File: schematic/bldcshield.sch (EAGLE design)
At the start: 39 parts, among them IC1 IR2101SMD, IC2 IR2101SMD, IC3 IR2101SMD, Q1 MOSFET-NCHANNELFDD8580, Q2 MOSFET-NCHANNELFDD8580, Q3 Shield, Q4 MOSFET-NCHANNELFDD8580, Q5 MOSFET-NCHANNELFDD8580, Q6 MOSFET-NCHANNELFDD8580, Q7 MOSFET-NCHANNELFDD8580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

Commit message: created new shield version in schematic based off lessons from Chinese controller.
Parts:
- removed JP1: (no value), SparkFun-Connectors:PINHD-2X3
- removed Q7: MOSFET-NCHANNELFDD8580, SparkFun:MOSFET-NCHANNELFDD8580
- removed U3: LM317DCY, Texas Instruments_By_element14_Batch_1:LM317DCY
- removed X1: MKDSN1,5/2-5,08, con-phoenix-508:MKDSN1,5/2-5,08
- removed X2: MKDSN1,5/3-5,08, con-phoenix-508:MKDSN1,5/3-5,08
- added +: Vcc, wirepad:3,81/1,4
- added -, BLDC1, BLDC2, BLDC3: (no value), wirepad:3,81/1,4
- added C3: 1000uF, SparkFun-Passives:CAP_POLPTH3
- added J1: (no value), SparkFun-Connectors:M02PTH
- added Q8: Shield, adafruit:ARDUINOR3-NOIOREF-NOTEXT
- added U1: V_REG_317SINK, SparkFun-PowerIC:V_REG_317SINK
- Q1, Q2, Q4, Q5, Q6: value MOSFET-NCHANNELFDD8580 -> BUZ11BV; device SparkFun:MOSFET-NCHANNELFDD8580 -> transistor-power:BUZ11BV
- Q3: value Shield -> BUZ11BV; device adafruit:ARDUINOR3-NOIOREF-NOTEXT -> transistor-power:BUZ11BV
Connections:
- removed net +3V3: Q3.3V
- removed net HI_1: IC1.HIN, Q3.D13
- removed net LO_1: IC1.LIN, Q3.D12
- removed net N$10: JP1.4, Q3.A1, R5.1
- new net N$2: R32.2, R33.1, U1.ADJ
- new net N$6: Q8.D2, R7.1
- new net N$8: IC1.LIN, Q8.D12
- net +12V: now also U1.OUT; no longer U3.OUTPUT, U3.OUTPUT_2
- net +5V: now also J1.2, Q8.5V; no longer JP1.1, Q3.5V, Q3.VIN
- net BLDC1: now also BLDC1.P; no longer X2-1.KL
- net BLDC2: now also BLDC2.P, Q3.S, Q4.D; no longer Q4.S, Q5.D, X2-2.KL
- net BLDC3: now also BLDC3.P, Q5.S, Q6.D; no longer Q6.S, Q7.D, X2-3.KL
- net CURRENT: now also Q4.S, Q6.S, Q8.A1; no longer Q3.A4/SDA, Q5.S, Q7.S
- net GND: now also -.P, C3.-, J1.1, Q8.GND, Q8.GND1, Q8.GND2; no longer JP1.5, Q3.GND, Q3.GND1, Q3.GND2, X1-2.KL
- net HI_2: now also Q8.D9; no longer Q3.D11
- net HI_3: now also Q8.D5; no longer Q3.D9
- net LOW_VOLTAGE: now also Q8.A0; no longer Q3.A3
- net LO_2: now also Q8.D8; no longer Q3.D10
- net LO_3: now also Q8.D13; no longer Q3.D8
- net N$1: now also Q3.G; no longer Q4.G
- net N$14: now also Q5.G; no longer Q6.G
- net N$15: now also Q6.G; no longer Q7.G
- net N$23: now also Q4.G; no longer Q5.G
- net N$4: now also IC1.HIN, Q8.D4; no longer JP1.2, Q3.A2, R7.1
- net N$5: now also Q8.D1, R5.1; no longer R32.2, R33.1, U3.ADJUST
- net N$7: now also Q8.D0; no longer JP1.6, Q3.A0
- net VCC: now also +.P, C3.+, Q3.D, Q5.D, U1.IN; no longer Q4.D, Q6.D, U3.INPUT, X1-1.KL
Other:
- moved on the sheet: C24, C25, R32, R33, R4, R5, R7

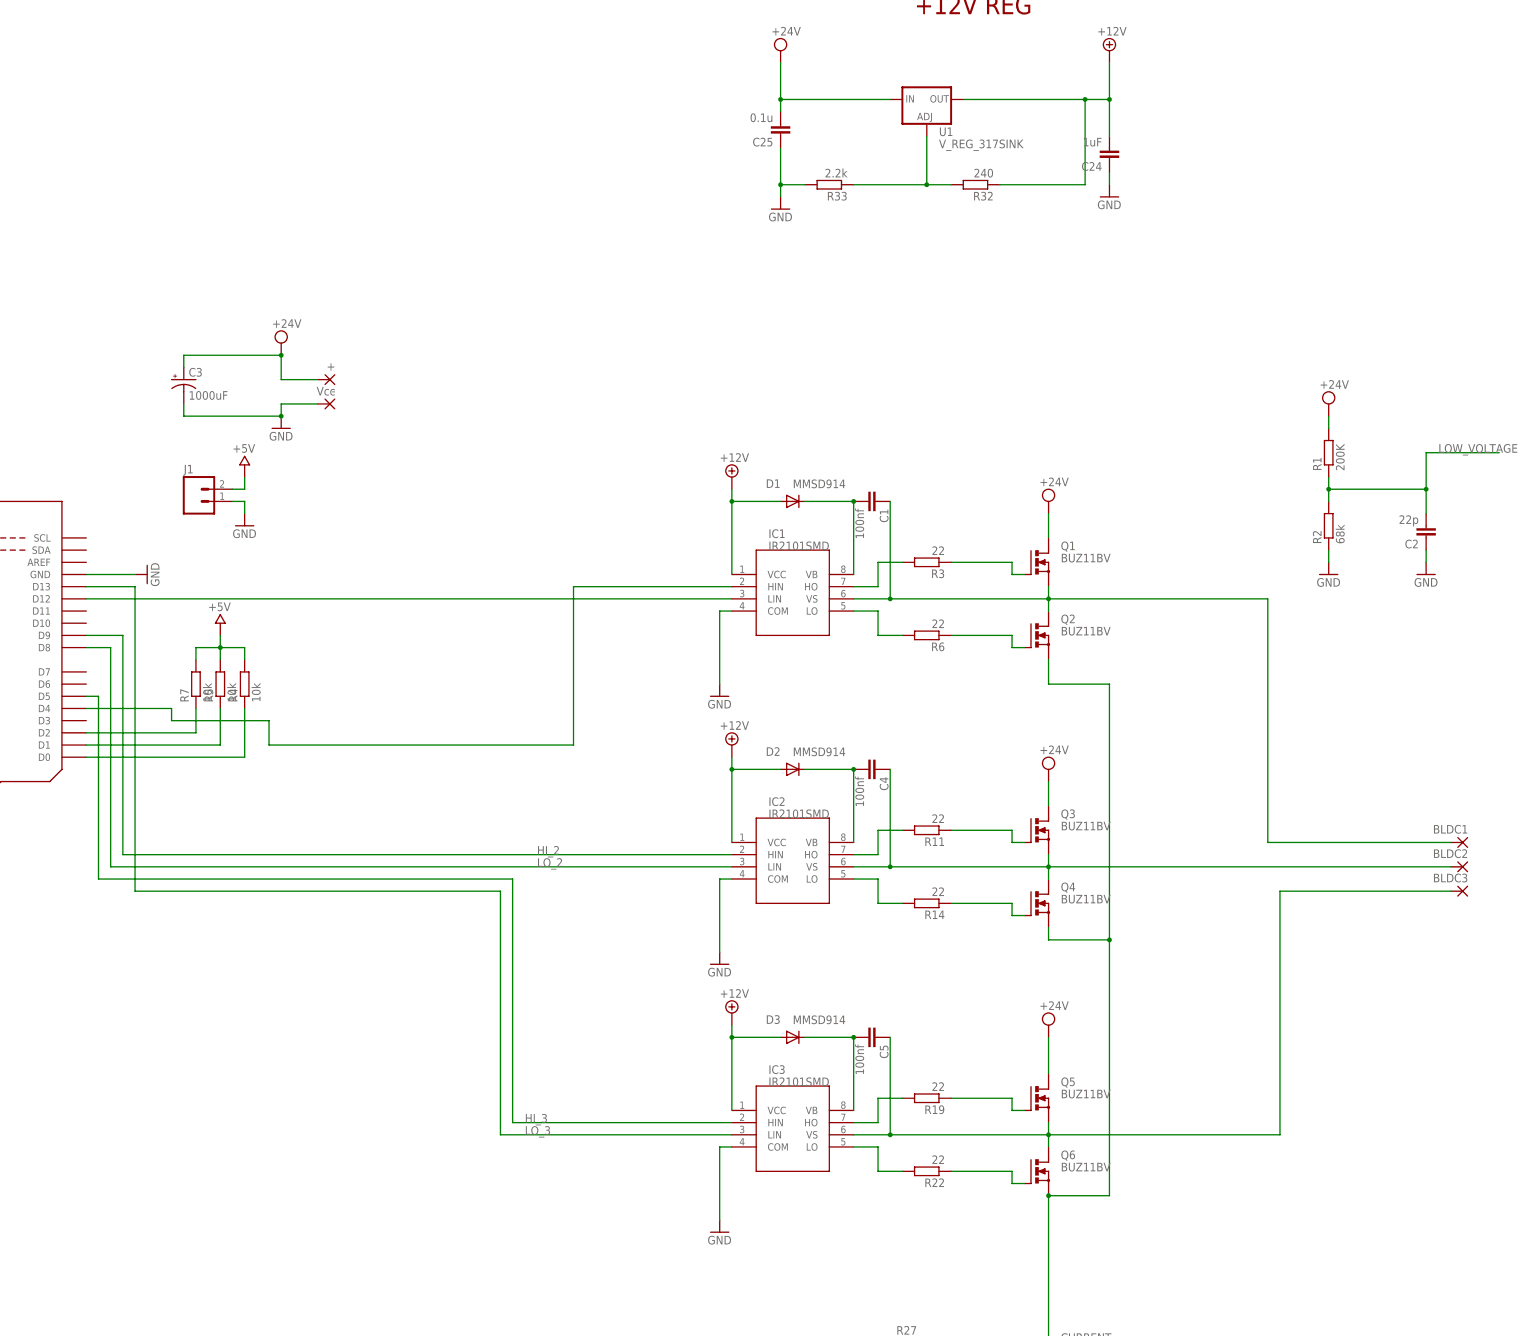
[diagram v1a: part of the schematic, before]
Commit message: working on new layout and swapped all transistors and wire pads.  Need to look at better IO assignment and redo power supply.
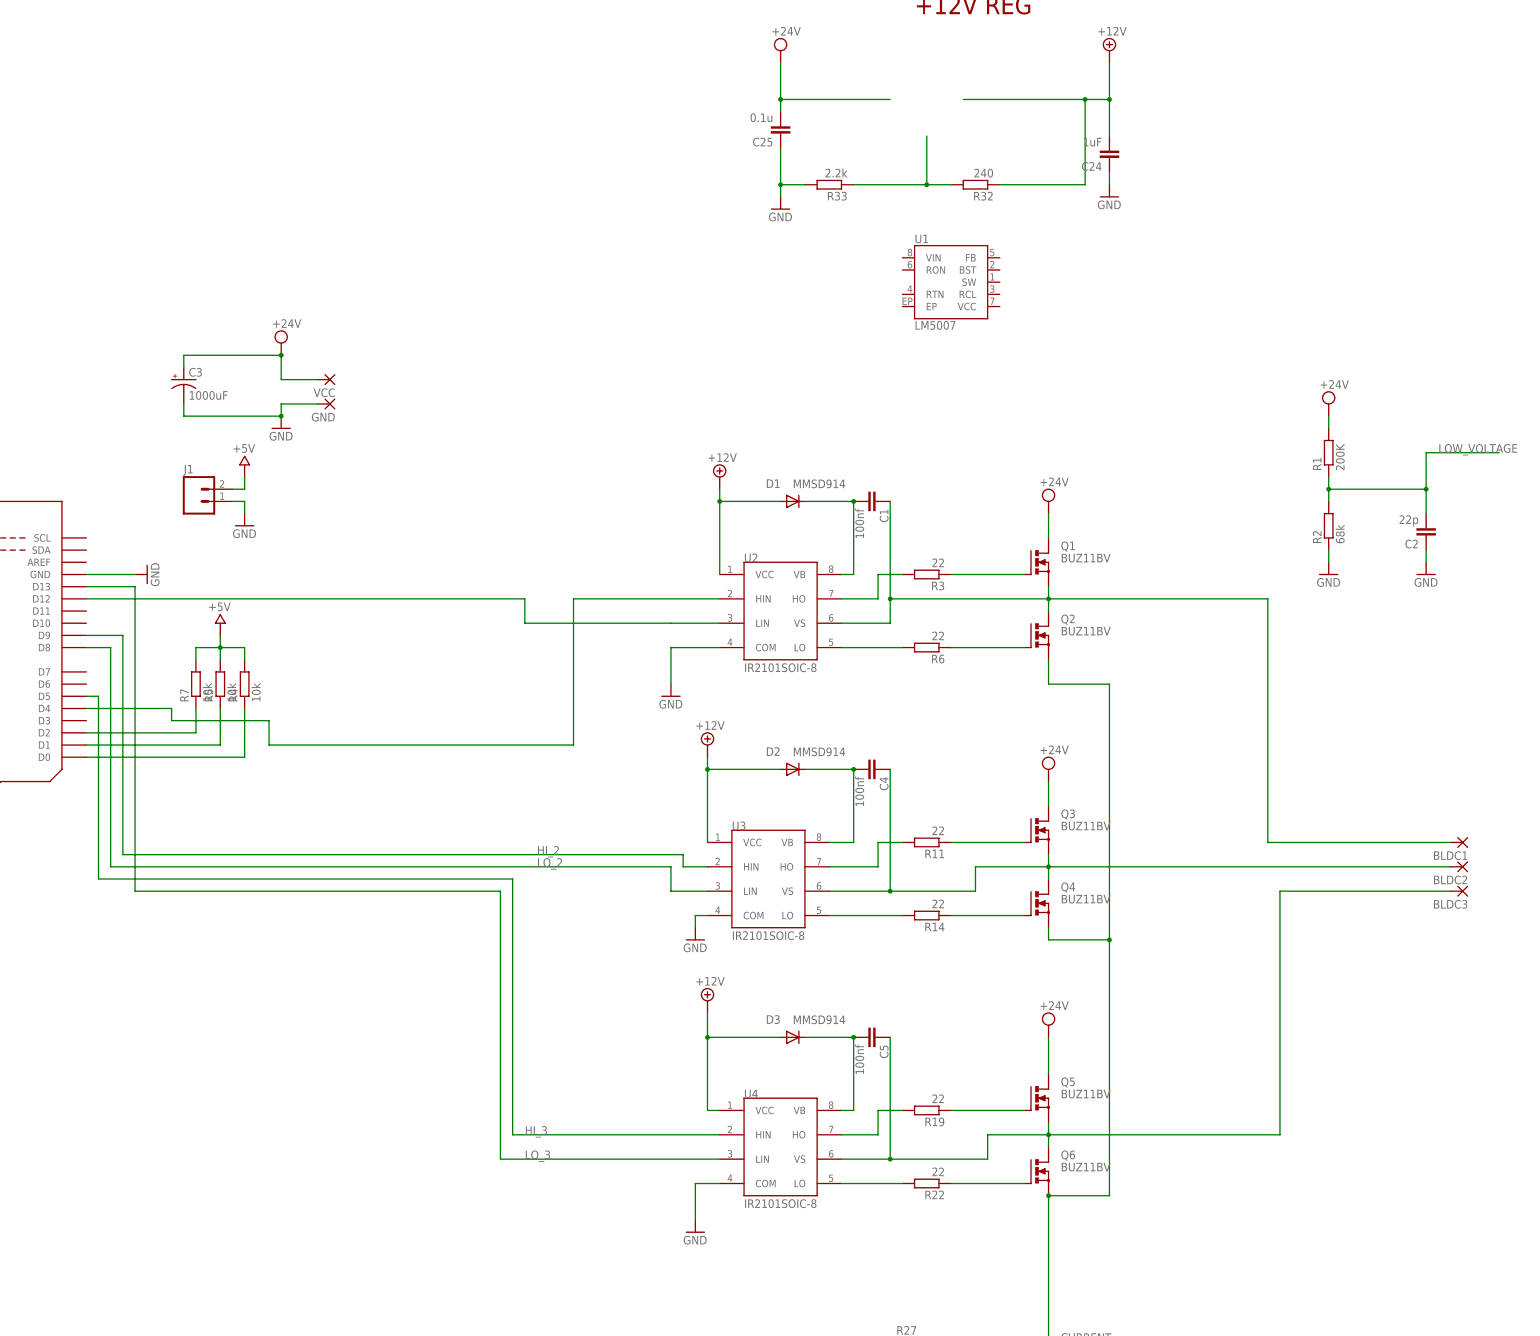
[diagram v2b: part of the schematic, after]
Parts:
- removed +: Vcc, wirepad:3,81/1,4
- removed -: (no value), wirepad:3,81/1,4
- removed IC1, IC2, IC3: IR2101SMD, IR:IR2101SMD
- added GND, VCC: WIREPAD4,16O1,6, wirepad:WIREPAD4,16O1,6
- added U2, U3, U4: IR2101SOIC-8, SnapEDA-Library:IR2101SOIC-8
- BLDC1, BLDC2, BLDC3: value (none) -> WIREPAD4,16O1,6; device wirepad:3,81/1,4 -> wirepad:WIREPAD4,16O1,6
- U1: value V_REG_317SINK -> LM5007; device SparkFun-PowerIC:V_REG_317SINK -> SparkFun-PowerIC:LM5007
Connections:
- removed net N$17: C5.2, D3.C, IC3.VB
- removed net N$25: C4.2, D2.C, IC2.VB
- removed net N$33: C1.2, D1.C, IC1.VB
- new net VB: C1.2, C4.2, C5.2, D1.C, D2.C, D3.C, U2.VB, U3.VB, U4.VB
- net +12V: now also U2.VCC, U3.VCC, U4.VCC; no longer IC1.VCC, IC2.VCC, IC3.VCC, U1.OUT
- net BLDC1: now also U2.VS; no longer IC1.VS
- net BLDC2: now also U3.VS; no longer IC2.VS
- net BLDC3: now also U4.VS; no longer IC3.VS
- net GND: now also GND.P, U2.COM, U3.COM, U4.COM; no longer -.P, IC1.COM, IC2.COM, IC3.COM
- net HI_2: now also U3.HIN; no longer IC2.HIN
- net HI_3: now also U4.HIN; no longer IC3.HIN
- net LO_2: now also U3.LIN; no longer IC2.LIN
- net LO_3: now also U4.LIN; no longer IC3.LIN
- net N$13: now also U4.HO; no longer IC3.HO
- net N$16: now also U4.LO; no longer IC3.LO
- net N$2: no longer U1.ADJ
- net N$21: now also U3.HO; no longer IC2.HO
- net N$24: now also U3.LO; no longer IC2.LO
- net N$29: no longer IC1.HO
- net N$32: no longer IC1.LO
- net N$4: now also U2.HIN; no longer IC1.HIN
- net N$8: now also U2.LIN; no longer IC1.LIN
- net VCC: now also VCC.P; no longer +.P, U1.IN
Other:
- moved on the sheet: R11, R14, R19, R22, R3, R6

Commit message: added pdfs for new parts
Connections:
- removed net N$29: R3.2
- removed net N$32: R6.2
- removed net VB: C1.2, C4.2, C5.2, D1.C, D2.C, D3.C, U2.VB, U3.VB, U4.VB
- new net N$10: R6.2, U2.LO
- new net N$11: R3.2, U2.HO
- new net VB1: C1.2, D1.C, U2.VB
- new net VB2: C4.2, D2.C, U3.VB
- new net VB3: C5.2, D3.C, U4.VB
- net HI_2: now also Q8.D10; no longer Q8.D9
- net HI_3: now also Q8.D9; no longer Q8.D5
- net LO_2: now also Q8.D6; no longer Q8.D8
- net LO_3: now also Q8.D5; no longer Q8.D13
- net N$4: now also Q8.D11; no longer Q8.D4
- net N$5: now also Q8.D4, R7.1; no longer Q8.D1, R5.1
- net N$6: now also Q8.D3, R5.1; no longer Q8.D2, R7.1
- net N$7: now also Q8.D2; no longer Q8.D0
- net N$8: now also Q8.D7; no longer Q8.D12
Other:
- moved on the sheet: R4, R5, R7

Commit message: generated gerbers for new boards.  might need some small tweaks on the keep out zones.
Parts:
- added C10, C11, C7: 100nF, SmartPrj:C-EUC1206
- added C12: 33uF, SparkFun-Capacitors:22UF-POLAR-PANASONIC_C-35V-20%
- added C6: 22uF, SparkFun-Capacitors:22UF-POLAR-PANASONIC_C-35V-20%
- added C9: 10nF, SmartPrj:C-EUC1206
- added D4: BAS70-05DPAK, SCHOTTKY:BAS70-05DPAK
- added D5: SMF43A, smf_11:SMF43A
- added D6: MBR0520LT, diode:MBR0520LT
- added L1: 100uH, SparkFun-Passives:INDUCTOR
- added R8: 1k, SmartPrj:R-EU_R1206
- added R9: 3.01k, SmartPrj:R-EU_R1206
- C24: value 1uF -> 100nF
- C25: value 0.1u -> 100nF
- R32: value 240 -> 100k
- R33: value 2.2k -> 200k
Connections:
- new net N$12: R33.1, U1.RON
- new net N$17: C9.2, U1.BST
- new net N$18: C7.2, U1.VCC
- new net N$19: C9.1, D6.C, L1.1, U1.SW
- new net N$20: R32.1, U1.RCL
- new net N$26: R8.1, R9.2, U1.FB
- net +12V: now also C10.2, C11.2, C12.+, L1.2, R9.1; no longer R32.1
- net GND: now also C10.1, C11.1, C12.-, C6.-, C7.1, D5.A, D6.A, R32.2, R8.2, U1.EP, U1.RTN; no longer R33.2
- net N$2: now also C25.2, C6.+, D4.K1K2, D5.C, R33.2, U1.VIN; no longer R32.2, R33.1
- net VCC: now also D4.A1, D4.A2; no longer C25.2
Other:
- moved on the sheet: C24, C25, R32, R33, U1

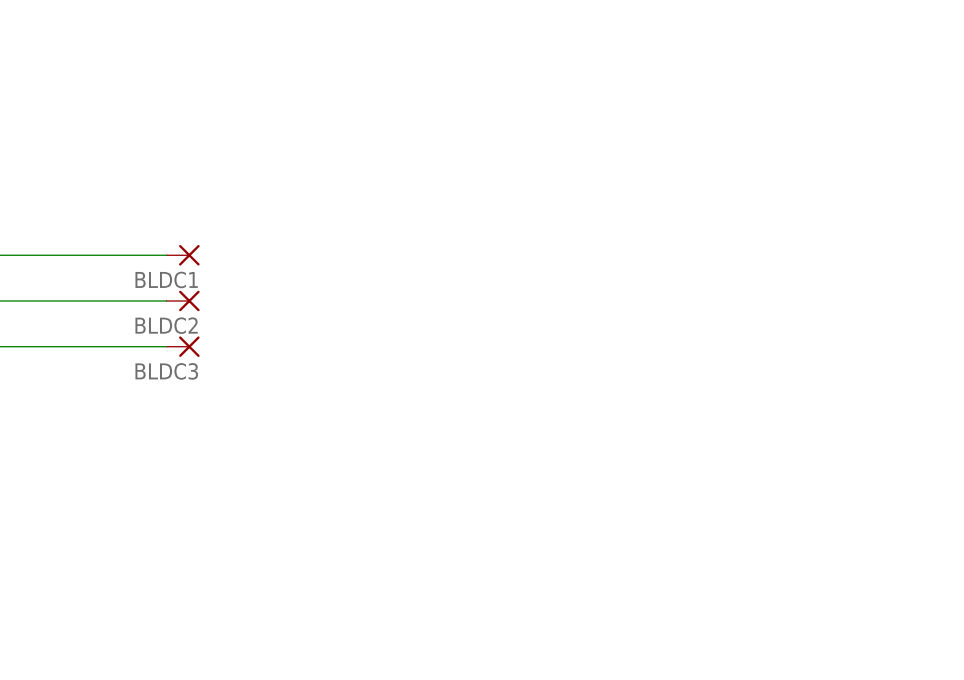
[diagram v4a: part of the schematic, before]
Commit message: added pdfs and added LED fixture to the LM5007 board.
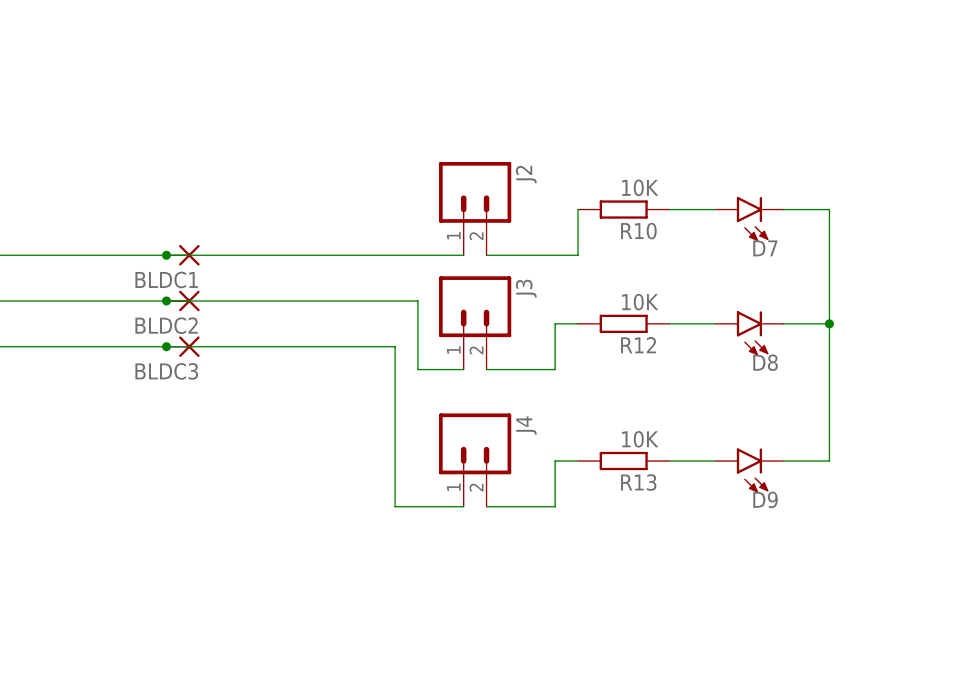
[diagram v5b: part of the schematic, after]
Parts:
- added D7, D8, D9: (no value), SparkFun-LED:LED5MM
- added J2, J3, J4: (no value), SparkFun-Connectors:M02PTH
- added R10, R12, R13: 10K, SmartPrj:R-EU_R1206
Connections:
- new net N$25: J2.2, R10.2
- new net N$27: J3.2, R12.2
- new net N$28: J4.2, R13.2
- new net N$29: D7.A, R10.1
- new net N$32: D8.A, R12.1
- new net N$33: D9.A, R13.1
- new net N$34: D7.C, D8.C, D9.C
- net BLDC1: now also J2.1
- net BLDC2: now also J3.1
- net BLDC3: now also J4.1
